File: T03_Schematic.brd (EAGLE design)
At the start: 100 x 80 mm, 52 parts, among them U2 ATMEGA328P_PDIP

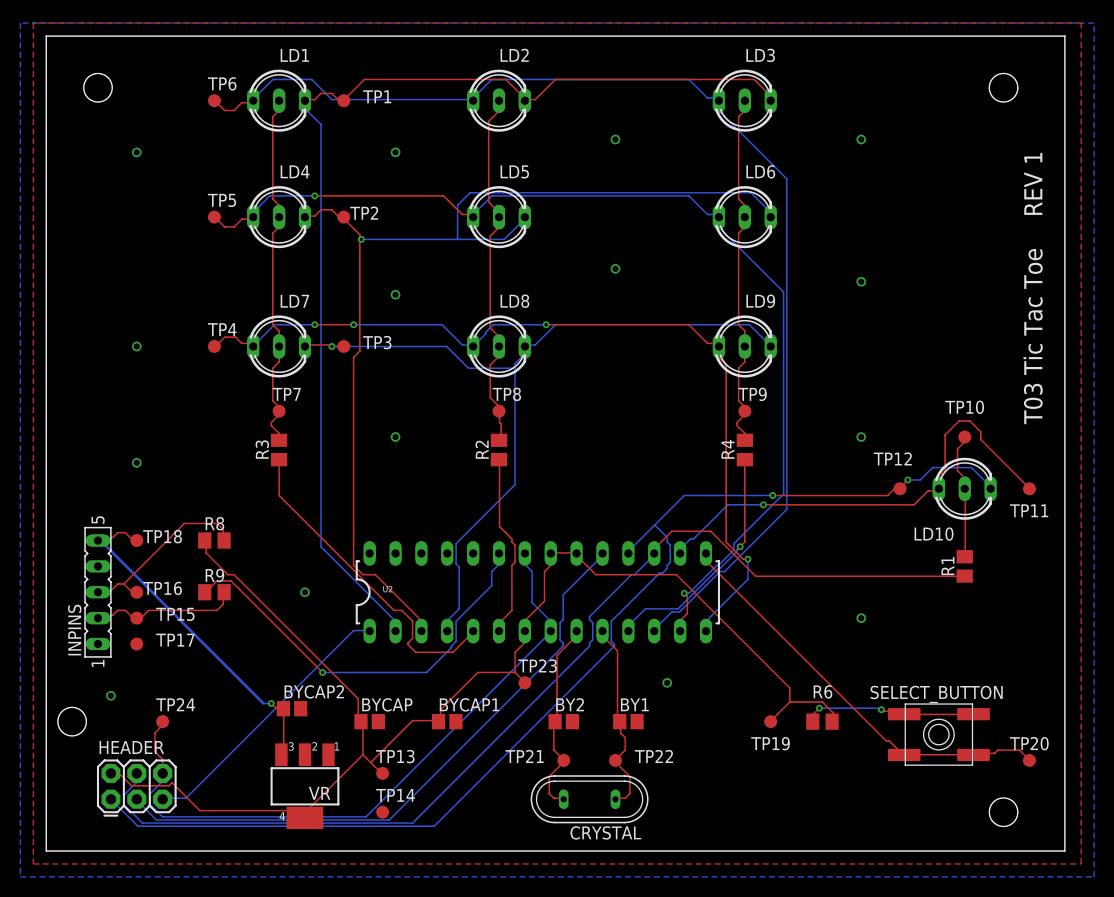
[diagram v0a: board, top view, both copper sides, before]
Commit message: Schematic has usb, new board
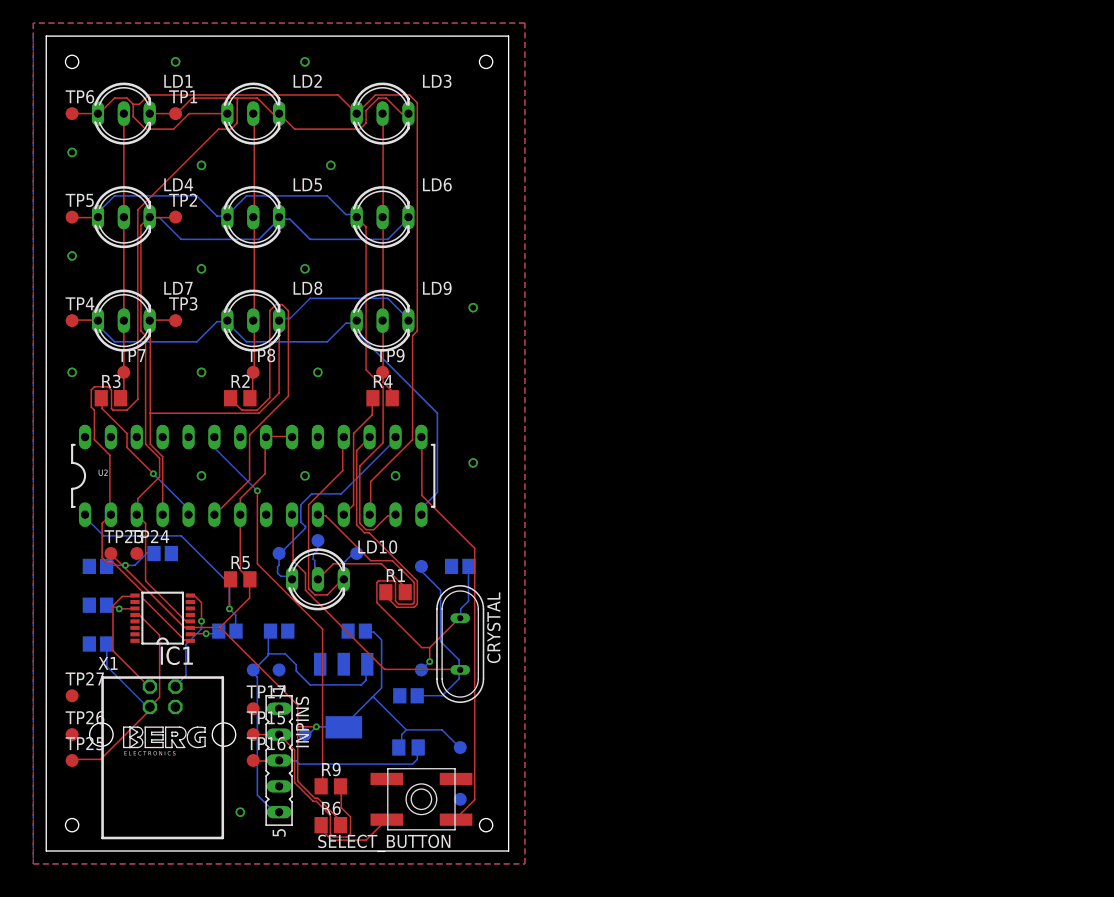
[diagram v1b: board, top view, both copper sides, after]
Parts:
- removed HEADER: AVR_SPI_PRG_6PTH, SparkFun-Connectors:2X3
- added BYCAP3, BYCAP4: 10u, adafruit:C0805
- added CAP, CAP1: 0.1u, adafruit:C0805
- added IC1: FT230XS, ftdichip:SSOP16
- added R5: 10k, adafruit:M0805
- added TP25, TP26, TP27: PTR1B1,27, testpad:B1,27
- added X1: (no value), con-berg:PN61729
- BY1, BY2: value 100n -> 10p
- BYCAP, BYCAP1: value 10u -> 0.1u
- moved TP11 73.9 mm to (22.9, 29.2), flipped to the bottom
- moved TP10 64.3 mm to (26.7, 30.5), flipped to the bottom
- moved LD10 64.1 mm to (26.7, 26.7)
- moved TP20 56.0 mm to (40.6, 5.08), flipped to the bottom
- moved R1 55.9 mm to (34.3, 25.4), turned to 0 degrees
- moved TP12 53.7 mm to (30.5, 29.2), flipped to the bottom
- moved SELECT_BUTTON 51.2 mm to (36.8, 5.08), turned to 180 degrees
- moved R6 49.3 mm to (27.9, 2.54)
- moved TP23 42.6 mm to (6.35, 29.2)
- moved R4 35.9 mm to (33.0, 44.5), turned to 0 degrees
- moved TP9 35.8 mm to (33.0, 47.0)
- moved LD9 35.7 mm to (33.0, 52.1)
- moved LD3 35.6 mm to (33.0, 72.4)
- moved LD6 35.6 mm to (33.0, 62.2)
- moved BYCAP1 32.5 mm to (11.4, 29.2), flipped to the bottom, turned to 180 degrees
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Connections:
- net N$13 renamed CRYSTAL-XTAL2
- net XTAL1 renamed CRYSTAL-XTAL1
- removed net N$11: HEADER.3, U2.19
- removed net N$12: HEADER.5, U2.1
- removed net RED1: LD1.AR, LD2.AR, LD3.AR, TP1.TP, U2.2
- removed net RED2: LD4.AR, LD5.AR, LD6.AR, TP2.TP, U2.3
- new net N$4: CAP.1, IC1.2
- new net N$5: IC1.8, X1.1
- new net N$7: IC1.9, X1.2
- new net RTS: CAP.2, R5.1, U2.1
- new net RXD: IC1.1, LD1.AR, LD2.AR, LD3.AR, TP1.TP, U2.2
- new net TXD: IC1.4, LD4.AR, LD5.AR, LD6.AR, TP2.TP, U2.3
- new net USBVCC: BYCAP3.1, IC1.12, TP25.TP, X1.3
- net CATH4: no longer HEADER.4
- net GND: now also BYCAP3.2, BYCAP4.2, CAP1.2, IC1.13, IC1.5, SELECT_BUTTON.A, SELECT_BUTTON.A', TP20.TP, TP24.TP, TP26.TP, TP27.TP, U2.22, U2.8, X1.4
- net N$2: no longer SELECT_BUTTON.B
- net N$8: now also CAP1.1, IC1.11; no longer HEADER.6, TP24.TP, U2.22, U2.8
- net PLAY2: no longer HEADER.1
- net SELECT: now also SELECT_BUTTON.B; no longer SELECT_BUTTON.A, SELECT_BUTTON.A', TP20.TP
- net VCC: now also BYCAP4.1, IC1.3, R5.2; no longer HEADER.2
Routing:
- net RED1: track 105.9 -> 0.00 mm
- net RED2: track 102.6 -> 0.00 mm, vias 1 -> 0
- net RXD: track 0.00 -> 101.4 mm
- net PLAY2: track 113.4 -> 24.1 mm, vias 2 -> 0
- net CATH4: track 102.9 -> 23.7 mm
- net TXD: track 0.00 -> 76.3 mm
- net N$8: track 65.4 -> 2.97 mm, vias 0 -> 1
- net N$11: track 60.8 -> 0.00 mm
- net VCC: track 132.8 -> 98.6 mm, vias 0 -> 2
- net GREN2: track 102.4 -> 68.4 mm, vias 2 -> 0
- net GREN3: track 85.2 -> 54.8 mm, vias 4 -> 0
- net USBVCC: track 0.00 -> 28.9 mm
- net N$12: track 27.3 -> 0.00 mm
- net RTS: track 0.00 -> 25.0 mm, vias 0 -> 1
- net CRYSTAL-XTAL1: track 19.7 -> 43.9 mm
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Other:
- board size 100 x 80 mm -> 45.4 x 80 mm
- board text removed: "REV 1"
- board text removed: "T03 Tic Tac Toe"

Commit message: final layout and schematic
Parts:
- removed SELECT_BUTTON: SPST_TACT-EVQQ2, adafruit:EVQ-Q2
- removed TP21, TP22: PTR1B1,27, testpad:B1,27
- added S1: DTS-6, switch-tact:DTS-6
- moved TP26 35.8 mm to (34.3, 27.9), flipped to the bottom
- moved BY2 28.4 mm to (22.9, 40.6)
- moved TP24 28.1 mm to (36.8, 31.8), flipped to the bottom
- moved CAP1 26.7 mm to (31.8, 22.9), flipped to the top, turned to 90 degrees
- moved BYCAP 24.4 mm to (29.2, 31.8), flipped to the top, turned to 90 degrees
- moved BYCAP1 23.6 mm to (25.4, 48.3), turned to 0 degrees
- moved TP7 22.9 mm to (7.62, 69.8)
- moved TP8 22.9 mm to (20.3, 69.8)
- moved LD10 22.6 mm to (44.5, 40.6)
- moved TP23 21.7 mm to (27.9, 26.7)
- moved TP9 21.6 mm to (34.3, 68.6)
- moved TP11 18.9 mm to (40.6, 35.6), flipped to the top
- moved TP27 18.9 mm to (20.3, 8.89)
- moved TP25 18.2 mm to (19.1, 16.5)
- moved BY1 18.0 mm to (27.9, 40.6)
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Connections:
- net N$7 renamed D-
- removed net N$5: IC1.8, X1.1
- new net D+: IC1.8, X1.3
- new net N$9: BYCAP1.1, U2.21
- net CRYSTAL-XTAL1: no longer TP21.TP
- net CRYSTAL-XTAL2: no longer TP22.TP
- net GND: now also S1.1, S1.2; no longer SELECT_BUTTON.A, SELECT_BUTTON.A'
- net N$2: now also S1.4; no longer SELECT_BUTTON.B'
- net SELECT: now also S1.3; no longer SELECT_BUTTON.B
- net USBVCC: now also X1.1; no longer X1.3
- net VCC: no longer BYCAP1.1, U2.21
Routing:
- net GND: track 0.00 -> 27.0 mm, vias 17 -> 26
- net CATH2: track 38.8 -> 15.2 mm
- net N$1: track 28.1 -> 44.6 mm
- net N$8: track 2.97 -> 19.0 mm, vias 1 -> 0
- net N$6: track 28.5 -> 43.4 mm
- net PLAY2: track 24.1 -> 38.6 mm
- net CRYSTAL-XTAL2: track 41.2 -> 27.9 mm, vias 1 -> 0
- net SELECTPIN: track 21.9 -> 9.02 mm
- net CRYSTAL-XTAL1: track 43.9 -> 32.7 mm
- net N$5: track 10.7 -> 0.00 mm, vias 1 -> 0
- net RED3: track 57.4 -> 47.0 mm
- net SELECT: track 40.5 -> 49.8 mm, vias 0 -> 1
- net D+: track 0.00 -> 9.22 mm
- net USBVCC: track 28.9 -> 37.2 mm, vias 0 -> 1
- net N$4: track 2.98 -> 11.0 mm
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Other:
- board size 45.4 x 80 mm -> 50.5 x 80 mm
- board text added: "T03-TIC TAC TOE-REV3 NOVEMBER 2014"
